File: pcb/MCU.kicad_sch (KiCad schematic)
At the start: 27 parts, among them J2 TC2030, J3 Conn_01x02_Pin, U2 LM4040DBZ-3, U6 FM24C64B, U7 STM32H563VITx, Y1 3225-25M-SR

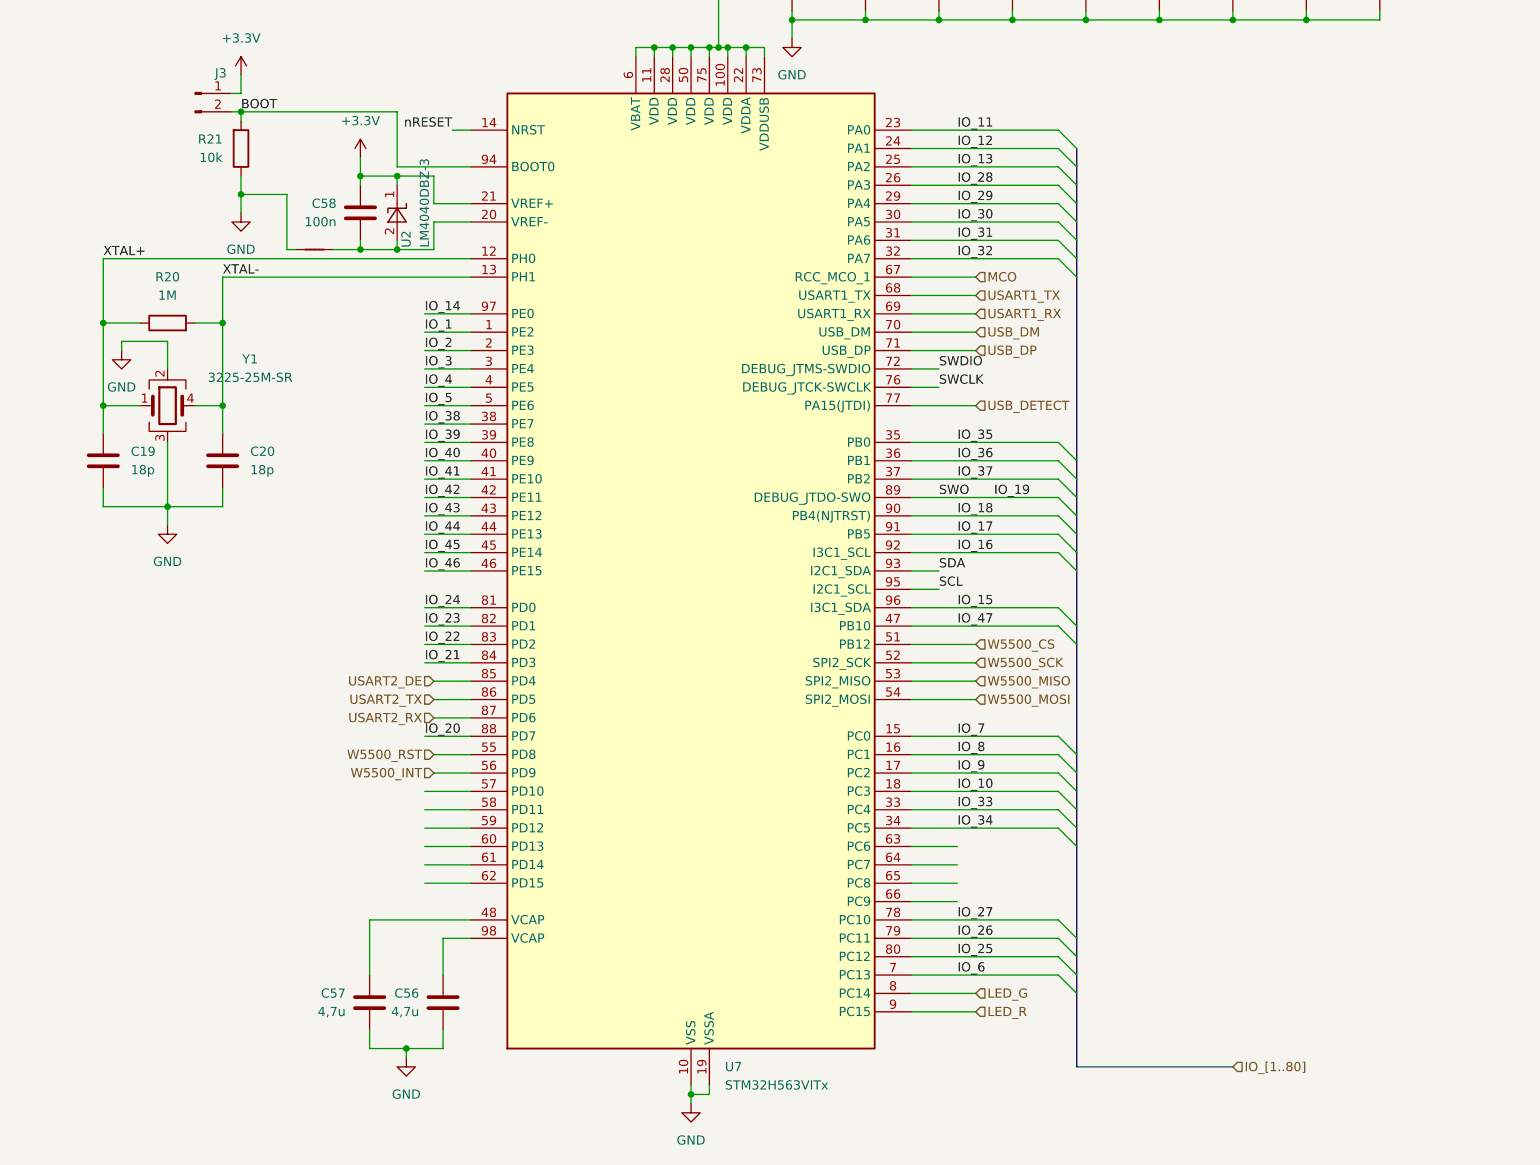
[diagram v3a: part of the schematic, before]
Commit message: Added SI5351C
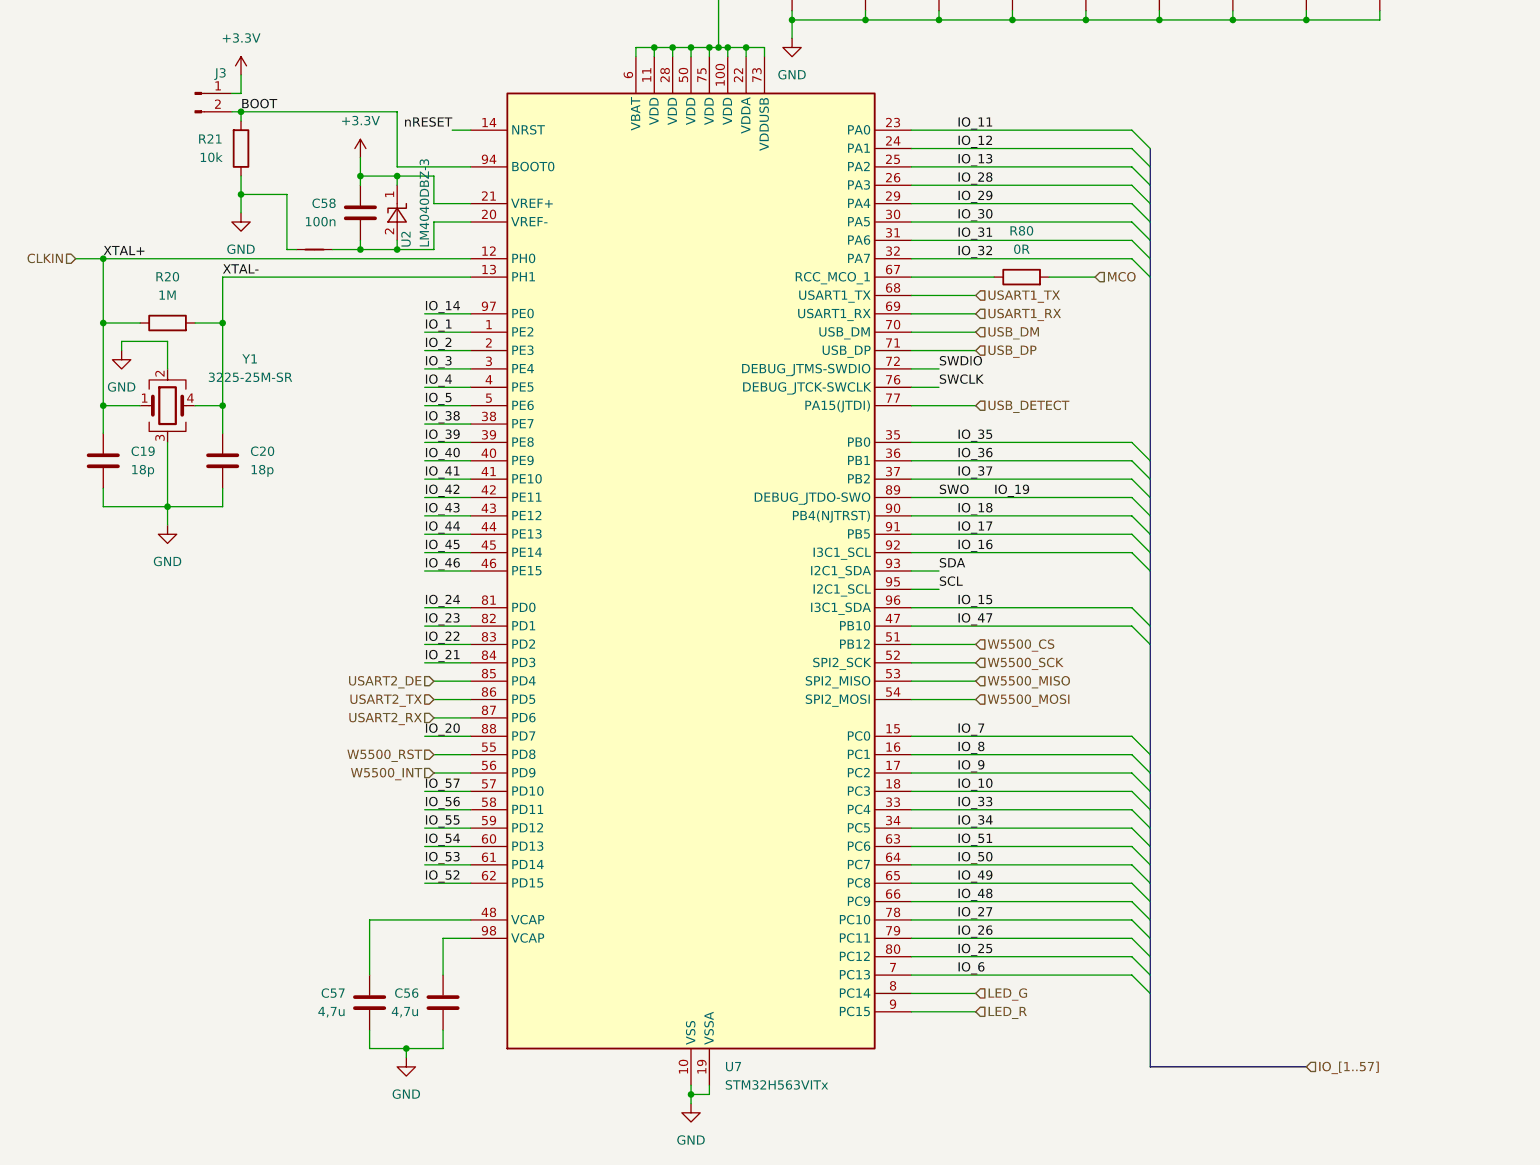
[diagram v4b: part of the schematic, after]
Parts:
- added R80: 0R, Resistor_SMD:R_0402_1005Metric_Pad0.72x0.64mm_HandSolder, symbol Device:R
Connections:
- net MCO: now also R80.2; no longer U7.67 (PA8)
- net IO_57: now reaches U7.57 (PD10)
- net IO_56: now reaches U7.58 (PD11)
- net IO_55: now reaches U7.59 (PD12)
- net IO_54: now reaches U7.60 (PD13)
- net IO_53: now reaches U7.61 (PD14)
- net IO_52: now reaches U7.62 (PD15)
- net IO_51: now reaches U7.63 (PC6)
- net IO_50: now reaches U7.64 (PC7)
- net IO_49: now reaches U7.65 (PC8)
- net IO_48: now reaches U7.66 (PC9)
- net XTAL+ renamed CLKIN
- new net: R80.1, U7.67 (PA8)

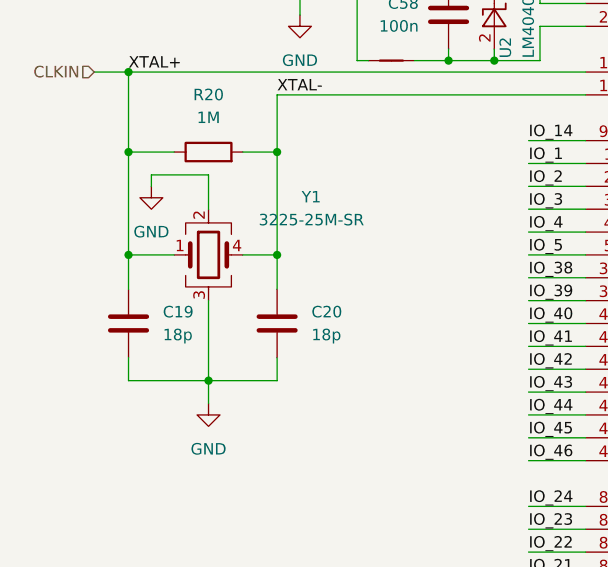
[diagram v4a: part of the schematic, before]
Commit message: More routing ...
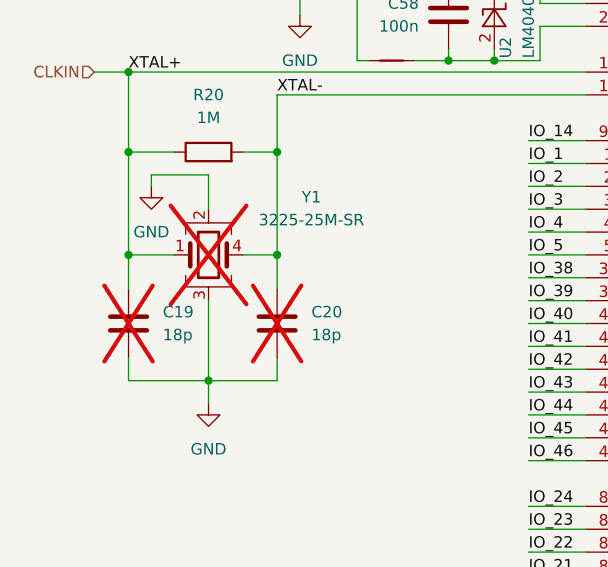
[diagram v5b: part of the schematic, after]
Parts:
- C19, C20, Y1: now not fitted; now left out of the parts list

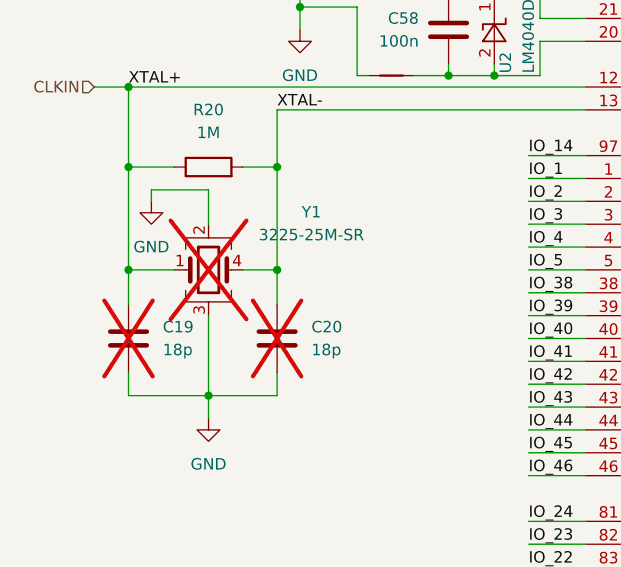
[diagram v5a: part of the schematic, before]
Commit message: Crystal footprint changed, routing and eth trafo to correct
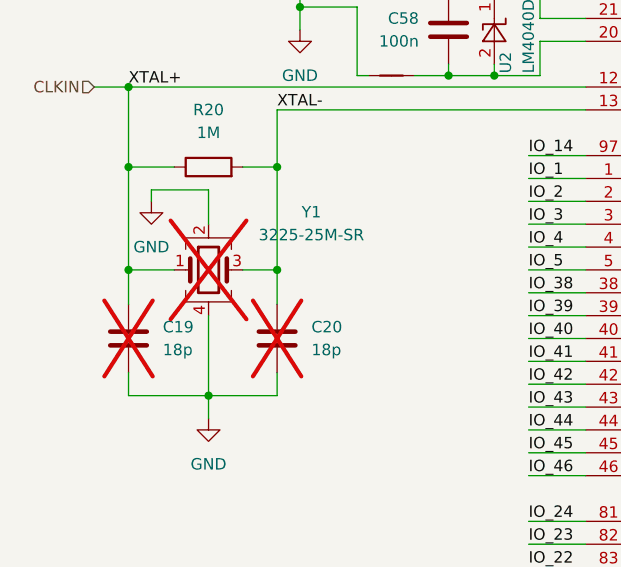
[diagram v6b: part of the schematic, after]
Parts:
- Y1: symbol Device:Crystal_GND23 -> Device:Crystal_GND24; now in the parts list
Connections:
- net GND: now also Y1.4; no longer Y1.3
- net XTAL-: now also Y1.3; no longer Y1.4
